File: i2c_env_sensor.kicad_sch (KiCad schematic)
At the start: 19 parts, among them J1 PH_4P_Header_3V3_I2C, U1 SHT40-AD1B-R3, U2 LPS22HBTR, U3 OPT3001DNPR

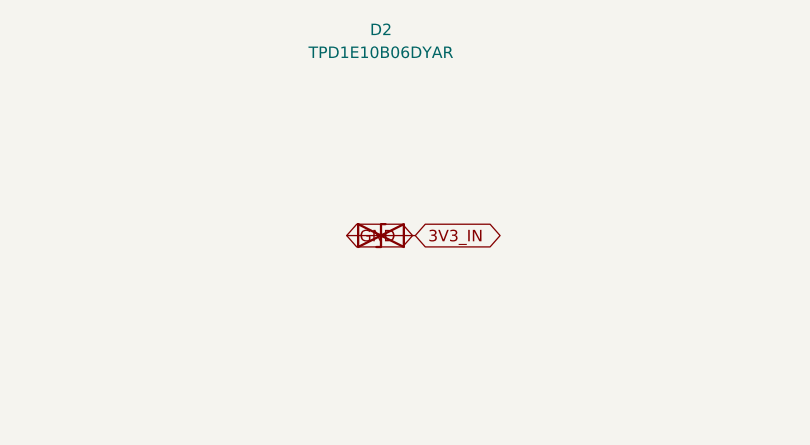
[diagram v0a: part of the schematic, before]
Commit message: Move the rail TVS to the cheaper package of the same part
TPD1E10B06 in TI's X1SON-2 (DPY) rather than SOT-5X3 (DYA): the same
die and the same datasheet, at $0.042 against $0.116 in ones, and 95,921
in stock against 8,682. The land pattern is DPY0002A read from the
datasheet already in evidence - two 0.3 x 0.5 mm pads 0.7 mm apart - and
the part now carries its own symbol, because the generic TVS symbol's
footprint filters are written for through-hole diode packages and pairing
them with this land pattern reads as a parity mismatch.

Checked every part against its manufacturer while here. TI publishes
Active/Production for all three of its parts in the package addenda dated
2025-2026, and Sensirion's catalogue reports SHT40 active; ST is not
reachable from this machine, so LPS22HB's status is unestablished rather
than confirmed. JLCPCB carries all ten, buyable, none idle or blacklisted.

$4.2084 to $4.1677 per board at 500.

Co-Authored-By: Claude Opus 5 <noreply@anthropic.com>
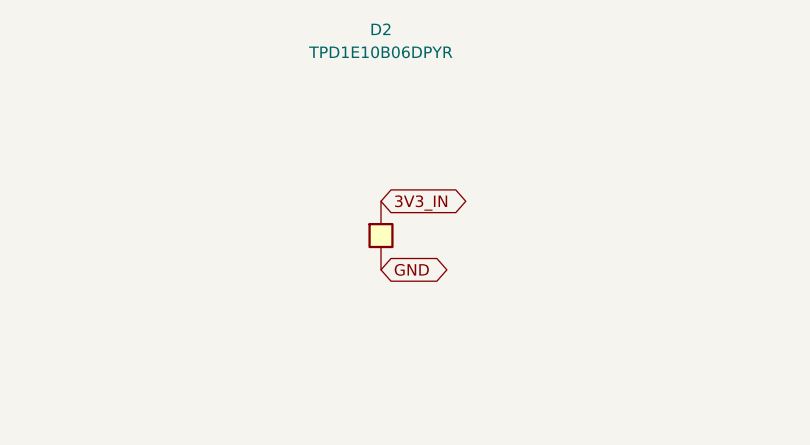
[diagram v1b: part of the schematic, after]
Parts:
- D2: value TPD1E10B06DYAR -> TPD1E10B06DPYR; footprint Diode_SMD:D_SOD-523 -> EnvSensorPod:Texas_X1SON-2_1.1x0.7mm_P0.7mm; symbol Device:D_TVS -> EnvSensorPod:TPD1E10B06; LCSC C3712135 -> C48260; MPN TPD1E10B06DYAR -> TPD1E10B06DPYR
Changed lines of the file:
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@@
 	)
 	(symbol
-		(lib_id "Device:D_TVS")
+		(lib_id "EnvSensorPod:TPD1E10B06")
 		(at 546.1 38.1 0)
 		(unit 1)
@@
 		(property
 			"Value"
-			"TPD1E10B06DYAR"
+			"TPD1E10B06DPYR"
 			(at 546.1 17.78 0)
 			(effects
@@
 		(property
 			"Footprint"
-			"Diode_SMD:D_SOD-523"
+			"EnvSensorPod:Texas_X1SON-2_1.1x0.7mm_P0.7mm"
 			(at 546.1 38.1 0)
 			(hide yes)
@@
 		(property
 			"MPN"
-			"TPD1E10B06DYAR"
+			"TPD1E10B06DPYR"
 			(at 546.1 38.1 0)
 			(hide yes)
@@
 		(property
 			"LCSC"
-			"C3712135"
+			"C48260"
 			(at 546.1 38.1 0)
 			(hide yes)
@@
 		"GND"
 		(shape bidirectional)
-		(at 542.29 38.1 0)
+		(at 546.1 41.91 0)
 		(effects
 			(font
@@
 		"3V3_IN"
 		(shape bidirectional)
-		(at 549.91 38.1 0)
-		(effects
-			(font
+		(at 546.1 34.29 0)
+		(effects
+			(font

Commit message: Fit resistors whose maker states a lifecycle, and close BOM.LIFECYCLE
The UNI-ROYAL thick-film parts were the only two of ten whose status
nobody publishes - not the manufacturer, not LCSC, not JLCPCB, not any
distributor carrying a Part Status field - so `unestablished` was the
honest record and unknown is not PASS. Both are replaced by parts whose
maker does state one.

  R1, R2  0402WGF2701TCE -> YAGEO RC0402FR-072K7L      C25885 -> C138017
  R3      0402WGF470KTCE -> Vishay Dale CRCW04024R70FKED  C25121 -> C482197

Same resistance, same +/-1%, same 0402 land pattern, same 62.5 mW and
50 V envelope, same -55 to 155 C range. The bodies are 1.0 x 0.5 mm as
before and 0.05 mm shorter (0.35 +/- 0.05 against the Uniroyal 0.45
maximum), which only relaxes clearance. Digi-Key states Part Status
Active for both, read 2026-09-11 and recorded in the snapshot with the
record number it was read from.

Choosing them was constrained twice over. Yageo's own 4.7 ohm part
(C137962) is out of stock in JLCPCB's assembly library despite the
storefront figure, so R3 went to Vishay, whose CRCW e3 is AEC-Q200
qualified and stocked at 8562. R1/R2 stayed with Yageo at 404034.

Nothing about the copper moved. The 135 track segments and 19 vias are
the identical set before and after; the board diff is 9 property fields
and the 12 UUIDs the canonicalize pass rederives from them. The routing
record re-recorded first attempt, adopting a board with the same sha256
it had before. The four front gerbers changed only by aperture D-code
renumbering - the aperture sets are identical - and STACK.GERBER_PARITY
confirms the geometry by symmetric difference.

Evidence: the Uniroyal specification leaves evidence/, and two frozen
datasheets replace it - YAGEO RC_L series V.14 and Vishay document
20035 revision 14-Apr-2026, both stating the 260 +/- 5 C for 10 +/- 1 s
resistance-to-soldering-heat the assembly records now cite. Eleven
frozen documents, thirty citations, all resolving.

Two corrections to ye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
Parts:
- R1, R2: LCSC C25885 -> C138017; MPN 0402WGF2701TCE -> RC0402FR-072K7L; Manufacturer UNI-ROYAL(Uniroyal Elec) -> YAGEO
- R3: LCSC C25121 -> C482197; MPN 0402WGF470KTCE -> CRCW04024R70FKED; Manufacturer UNI-ROYAL(Uniroyal Elec) -> Vishay Intertech
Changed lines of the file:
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@@
 		(property
 			"MPN"
-			"0402WGF2701TCE"
+			"RC0402FR-072K7L"
 			(at 38.1 101.6 0)
 			(hide yes)
@@
 		(property
 			"Manufacturer"
-			"UNI-ROYAL(Uniroyal Elec)"
+			"YAGEO"
 			(at 38.1 101.6 0)
 			(hide yes)
@@
 		(property
 			"LCSC"
-			"C25885"
+			"C138017"
 			(at 38.1 101.6 0)
 			(hide yes)
@@
 		(property
 			"MPN"
-			"0402WGF2701TCE"
+			"RC0402FR-072K7L"
 			(at 101.6 101.6 0)
 			(hide yes)
@@
 		(property
 			"Manufacturer"
-			"UNI-ROYAL(Uniroyal Elec)"
+			"YAGEO"
 			(at 101.6 101.6 0)
 			(hide yes)
@@
 		(property
 			"LCSC"
-			"C25885"
+			"C138017"
 			(at 101.6 101.6 0)
 			(hide yes)
@@
 		(property
 			"MPN"
-			"0402WGF470KTCE"
+			"CRCW04024R70FKED"
 			(at 165.1 101.6 0)
 			(hide yes)
@@
 		(property
 			"Manufacturer"
-			"UNI-ROYAL(Uniroyal Elec)"
+			"Vishay Intertech"
 			(at 165.1 101.6 0)
 			(hide yes)
@@
 		(property
 			"LCSC"
-			"C25121"
-			(at 165.1 101.6 0)
-			(hide yes)
+			"C482197"
+			(at 165.1 101.6 0)
+			(hide yes)
